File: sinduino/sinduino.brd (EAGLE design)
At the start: 60 x 37 mm, 34 parts, among them IC1 IC_UC_ATMEGA32U4-TQFP44, IC2 TS2940CT5TV, Q1 16000, X1 MINI-USB-32005-301

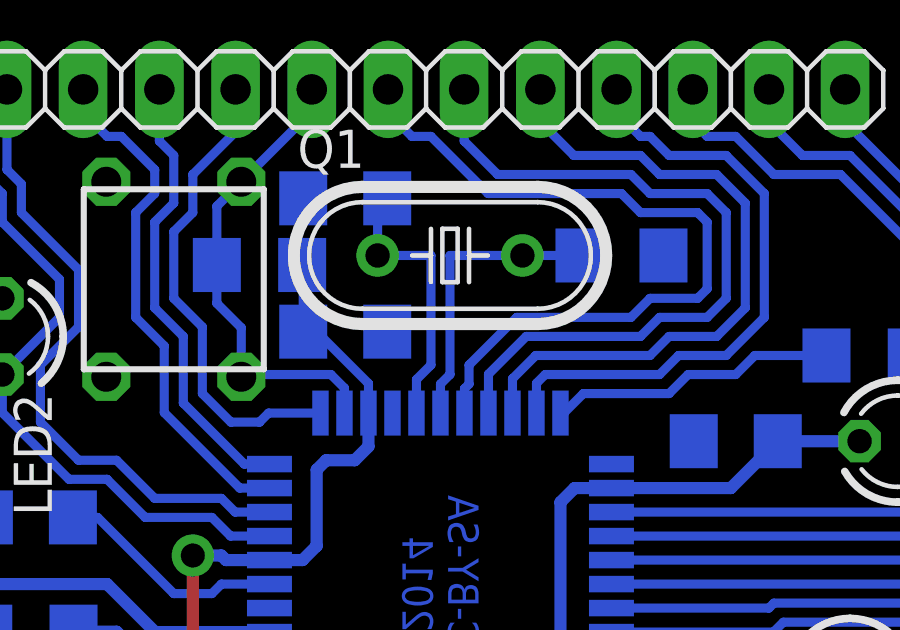
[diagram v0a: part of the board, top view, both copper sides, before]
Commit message: name some unnamed signals
and improve xtal routing
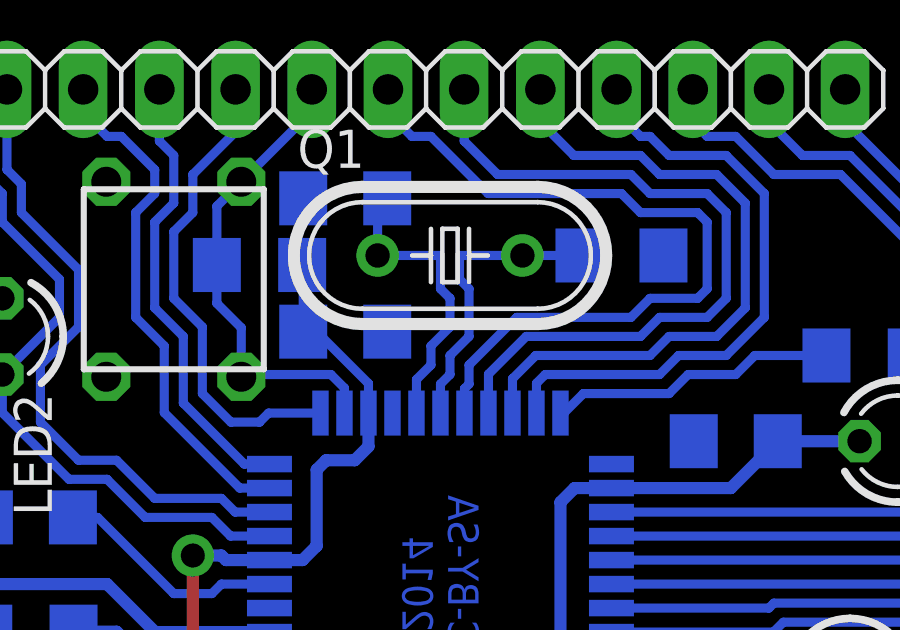
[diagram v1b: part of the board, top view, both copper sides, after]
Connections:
- net N$1 renamed D10
- net N$12 renamed D9
- net N$13 renamed D8
- net N$2 renamed TXLED
- net N$3 renamed XTAL1
- net N$4 renamed XTAL2
- net N$6 renamed UCAP
- net N$8 renamed D+
- net N$9 renamed D-
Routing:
- net XTAL2: track 9.27 -> 9.99 mm
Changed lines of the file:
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@@
 <setting verticaltext="up"/>
 </settings>
-<grid distance="50" unitdist="mil" unit="mil" style="dots" multiple="1" display="yes" altdistance="25" altunitdist="mil" altunit="mil"/>
+<grid distance="12.5" unitdist="mil" unit="mil" style="dots" multiple="1" display="yes" altdistance="25" altunitdist="mil" altunit="mil"/>
 <layers>
 <layer number="1" name="Top" color="4" fill="1" visible="yes" active="yes"/>
@@
 </polygon>
 </signal>
-<signal name="N$3">
+<signal name="XTAL1">
 <contactref element="C8" pad="2"/>
 <contactref element="IC1" pad="P17"/>
@@
 <wire x1="36.83" y1="22.21" x2="36.83" y2="23.1775" width="0.3048" layer="16"/>
 <wire x1="36.83" y1="23.1775" x2="37.1475" y2="23.495" width="0.3048" layer="16"/>
-<wire x1="37.1475" y1="23.495" x2="37.1475" y2="27.46375" width="0.3048" layer="16"/>
-<wire x1="37.1475" y1="27.46375" x2="39.5605" y2="27.46375" width="0.3048" layer="16"/>
 <wire x1="39.5605" y1="27.46375" x2="41.4625" y2="27.46375" width="0.3048" layer="16"/>
-</signal>
-<signal name="N$4">
+<wire x1="37.1475" y1="23.495" x2="37.1475" y2="24.13" width="0.3048" layer="16"/>
+<wire x1="37.465" y1="27.46375" x2="39.5605" y2="27.46375" width="0.3048" layer="16"/>
+<wire x1="37.1475" y1="24.13" x2="37.7825" y2="24.765" width="0.3048" layer="16"/>
+<wire x1="37.7825" y1="24.765" x2="37.7825" y2="26.3525" width="0.3048" layer="16"/>
+<wire x1="37.7825" y1="26.3525" x2="37.465" y2="26.67" width="0.3048" layer="16"/>
+<wire x1="37.465" y1="26.67" x2="37.465" y2="27.46375" width="0.3048" layer="16"/>
+</signal>
+<signal name="XTAL2">
 <contactref element="IC1" pad="P16"/>
 <contactref element="C9" pad="2"/>
@@
 <wire x1="36.03" y1="22.21" x2="36.03" y2="23.33" width="0.3048" layer="16"/>
 <wire x1="36.03" y1="23.33" x2="36.5125" y2="23.8125" width="0.3048" layer="16"/>
-<wire x1="36.5125" y1="23.8125" x2="36.5125" y2="27.46375" width="0.3048" layer="16"/>
-<wire x1="36.5125" y1="27.46375" x2="34.7345" y2="27.46375" width="0.3048" layer="16"/>
 <wire x1="34.7345" y1="27.46375" x2="34.7345" y2="29.04825" width="0.3048" layer="16"/>
 <wire x1="34.7345" y1="29.04825" x2="35.055" y2="29.36875" width="0.3048" layer="16"/>
-</signal>
-<signal name="N$6">
+<wire x1="36.5125" y1="23.8125" x2="36.5125" y2="24.4475" width="0.3048" layer="16"/>
+<wire x1="36.83" y1="27.46375" x2="34.7345" y2="27.46375" width="0.3048" layer="16"/>
+<wire x1="36.5125" y1="24.4475" x2="37.1475" y2="25.0825" width="0.3048" layer="16"/>
+<wire x1="37.1475" y1="25.0825" x2="37.1475" y2="26.035" width="0.3048" layer="16"/>
+<wire x1="37.1475" y1="26.035" x2="36.83" y2="26.3525" width="0.3048" layer="16"/>
+<wire x1="36.83" y1="26.3525" x2="36.83" y2="27.46375" width="0.3048" layer="16"/>
+</signal>
+<signal name="UCAP">
 <contactref element="IC1" pad="P6"/>
 <contactref element="C10" pad="1"/>
@@
 <wire x1="29.3755" y1="29.1055" x2="29.3755" y2="27.14625" width="0.3048" layer="16"/>
 </signal>
-<signal name="N$8">
+<signal name="D+">
 <contactref element="R8" pad="2"/>
 <contactref element="IC1" pad="P4"/>
@@
 <wire x1="27.3175" y1="14.91" x2="25.7175" y2="16.51" width="0.4064" layer="16"/>
 </signal>
-<signal name="N$9">
+<signal name="D-">
 <contactref element="IC1" pad="P3"/>
 <contactref element="R7" pad="2"/>
@@
 <wire x1="56.515" y1="25.7175" x2="50.32" y2="31.9125" width="0.3048" layer="16"/>
 </signal>
-<signal name="N$2">
+<signal name="TXLED">
 <contactref element="IC1" pad="P22"/>
 <contactref element="R6" pad="1"/>
@@
 <wire x1="49.8475" y1="8.255" x2="48.5775" y2="6.985" width="0.3048" layer="16"/>
 </signal>
-<signal name="N$1">
+<signal name="D10">
 <contactref element="JP3" pad="3"/>
 <contactref element="IC1" pad="P30"/>
@@
 <wire x1="48.895" y1="6.35" x2="50.165" y2="7.62" width="0.3048" layer="16"/>
 </signal>
-<signal name="N$12">
+<signal name="D9">
 <contactref element="IC1" pad="P29"/>
 <contactref element="JP3" pad="2"/>
@@
 <wire x1="49.2125" y1="5.715" x2="50.4825" y2="6.985" width="0.3048" layer="16"/>
 </signal>
-<signal name="N$13">
+<signal name="D8">
 <contactref element="JP3" pad="1"/>
 <contactref element="IC1" pad="P28"/>

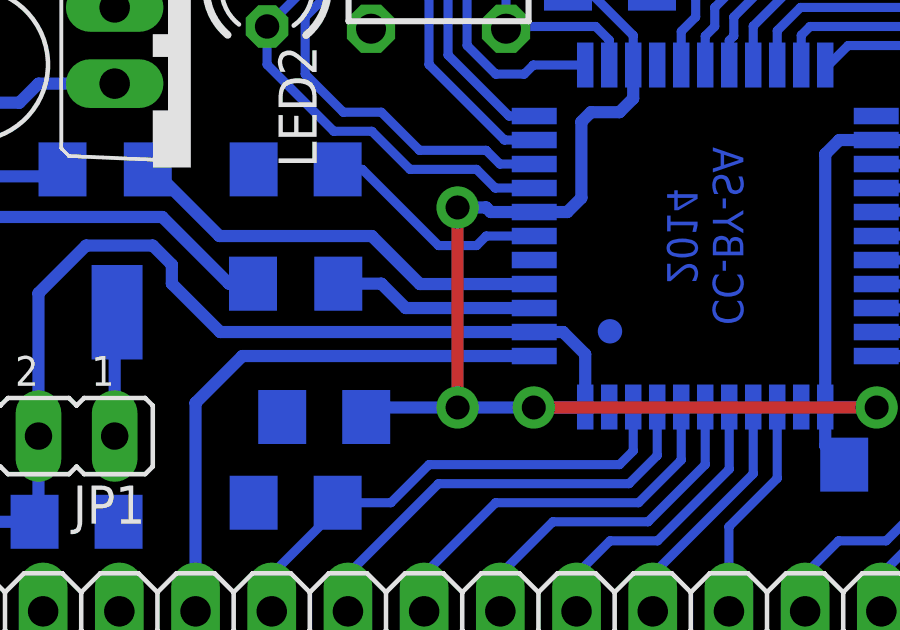
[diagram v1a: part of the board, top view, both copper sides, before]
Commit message: adapt resistor values and move one via
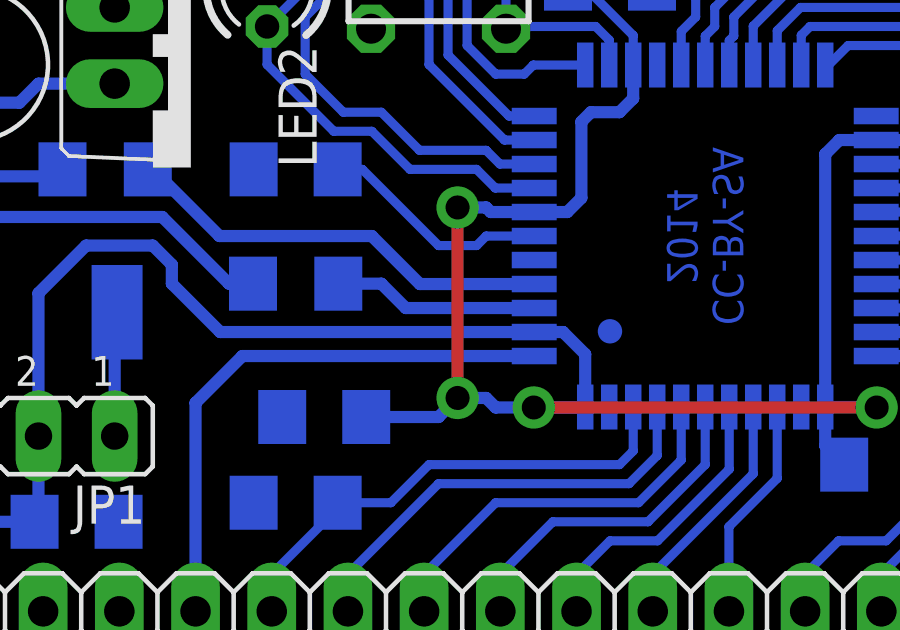
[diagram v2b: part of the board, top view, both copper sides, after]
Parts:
- R1, R2, R4, R6: value 680 -> 1k5
- R5: value 3k9 -> 10k
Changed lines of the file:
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@@
 <setting verticaltext="up"/>
 </settings>
-<grid distance="12.5" unitdist="mil" unit="mil" style="dots" multiple="1" display="yes" altdistance="25" altunitdist="mil" altunit="mil"/>
+<grid distance="50" unitdist="mil" unit="mil" style="dots" multiple="1" display="yes" altdistance="0.025" altunitdist="inch" altunit="mil"/>
 <layers>
 <layer number="1" name="Top" color="4" fill="1" visible="yes" active="yes"/>
@@
 <element name="JP2" library="pinhead" package="1X17" value="" x="30" y="33"/>
 <element name="JP3" library="pinhead" package="1X17" value="" x="30" y="4" rot="R180"/>
-<element name="R6" library="rcl" package="R1206" value="680" x="51.1175" y="24.13" rot="MR180"/>
+<element name="R6" library="rcl" package="R1206" value="1k5" x="51.1175" y="24.13" rot="MR180"/>
 <element name="LED4" library="led" package="LED3MM" value="yellow" x="52.07" y="21.2725"/>
-<element name="R5" library="rcl" package="R1206" value="3k9" x="46.6725" y="10.4775" rot="MR90"/>
+<element name="R5" library="rcl" package="R1206" value="10k" x="46.6725" y="10.4775" rot="MR90"/>
 <element name="IC2" library="n39" package="TO220V" value="TS2940CT5TV" x="19.685" y="24.13" rot="R270">
 <attribute name="REICHELT" value="LM 2940 CT5" x="19.685" y="24.13" size="1.778" layer="27" rot="R270" display="off"/>
@@
 </element>
 <element name="LED1" library="led" package="LED3MM" value="green" x="3.81" y="9.525" rot="R180"/>
-<element name="R1" library="rcl" package="R1206" value="680" x="10.795" y="6.985" rot="MR0"/>
-<element name="R2" library="rcl" package="R1206" value="680" x="16.8275" y="29.5275" rot="MR0"/>
+<element name="R1" library="rcl" package="R1206" value="1k5" x="10.795" y="6.985" rot="MR0"/>
+<element name="R2" library="rcl" package="R1206" value="1k5" x="16.8275" y="29.5275" rot="MR0"/>
 <element name="LED2" library="led" package="LED3MM" value="orange" x="22.225" y="24.765" rot="R270"/>
-<element name="R4" library="rcl" package="R1206" value="680" x="50.4825" y="10.4775" rot="MR0"/>
+<element name="R4" library="rcl" package="R1206" value="1k5" x="50.4825" y="10.4775" rot="MR0"/>
 <element name="LED3" library="led" package="LED3MM" value="red" x="50.4825" y="13.335"/>
 </elements>
@@
 <wire x1="42.545" y1="10.795" x2="42.53" y2="10.81" width="0.4064" layer="16"/>
 <wire x1="42.53" y1="10.81" x2="40.83" y2="10.81" width="0.4064" layer="16"/>
-<wire x1="31.115" y1="10.795" x2="28.575" y2="10.795" width="0.4064" layer="16"/>
-<wire x1="28.575" y1="17.4625" x2="28.575" y2="10.795" width="0.4064" layer="1"/>
+<wire x1="28.575" y1="17.4625" x2="28.575" y2="11.1125" width="0.4064" layer="1"/>
 <via x="28.575" y="17.4625" extent="1-16" drill="0.8" shape="octagon"/>
-<via x="28.575" y="10.795" extent="1-16" drill="0.8" shape="octagon"/>
-<wire x1="28.575" y1="10.795" x2="25.8475" y2="10.795" width="0.4064" layer="16"/>
-<wire x1="25.8475" y1="10.795" x2="25.53" y2="10.4775" width="0.4064" layer="16"/>
+<via x="28.575" y="11.1125" extent="1-16" drill="0.8" shape="octagon"/>
 <wire x1="31.13" y1="17.31" x2="32.2325" y2="17.31" width="0.4064" layer="16"/>
 <wire x1="31.13" y1="13.31" x2="20.6625" y2="13.31" width="0.4064" layer="16"/>
@@
 <wire x1="12.065" y1="6.985" x2="12.217" y2="6.985" width="0.4064" layer="16"/>
 <wire x1="14.475" y1="6.985" x2="12.217" y2="6.985" width="0.4064" layer="16"/>
+<wire x1="25.53" y1="10.4775" x2="27.94" y2="10.4775" width="0.4064" layer="16"/>
+<wire x1="27.94" y1="10.4775" x2="28.575" y2="11.1125" width="0.4064" layer="16"/>
+<wire x1="28.575" y1="11.1125" x2="29.5275" y2="11.1125" width="0.4064" layer="16"/>
+<wire x1="29.5275" y1="11.1125" x2="29.845" y2="10.795" width="0.4064" layer="16"/>
+<wire x1="29.845" y1="10.795" x2="31.115" y2="10.795" width="0.4064" layer="16"/>
 </signal>
 <signal name="GND" class="1">

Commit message: replace mini usb connector and fix #3
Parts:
- X1: value MINI-USB-32005-301 -> USB_B_M-MINS; device con-cypressindustries:32005-301 -> n39:LUMBERG_2486-01
- moved X1 2.63 mm to (5.85, 15.9), turned to 90 degrees
- moved LED1 1.31 mm to (5.08, 9.84), turned to 90 degrees
- moved F1 0.45 mm to (14.9, 13.7)
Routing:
- net N$16: track 27.5 -> 23.8 mm
- net VCC: track 147.8 -> 145.6 mm
- net N$7: track 6.50 -> 8.50 mm
- net N$10: track 5.36 -> 4.01 mm
- net N$14: track 6.18 -> 4.95 mm
- net N$5: track 13.9 -> 14.7 mm

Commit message: change XTAL capicator values to 22p (you can not buy 18p)
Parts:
- C8, C9: value 18p -> 22p
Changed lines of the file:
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@@
 <element name="C6" library="rcl" package="C1206" value="100n" x="24.13" y="10.4775" rot="MR0"/>
 <element name="C7" library="rcl" package="C1206" value="100n" x="23.1775" y="7.62" rot="MR0"/>
-<element name="C8" library="rcl" package="C1206" value="18p" x="42.8625" y="27.46375" rot="MR0"/>
-<element name="C9" library="rcl" package="C1206" value="18p" x="33.655" y="29.36875" rot="MR180"/>
+<element name="C8" library="rcl" package="C1206" value="22p" x="42.8625" y="27.46375" rot="MR0"/>
+<element name="C9" library="rcl" package="C1206" value="22p" x="33.655" y="29.36875" rot="MR180"/>
 <element name="C10" library="rcl" package="C1206" value="1u" x="23.1775" y="18.7325" rot="MR0"/>
 <element name="C11" library="rcl" package="C1206" value="1u" x="15.875" y="6.985" rot="MR180"/>
